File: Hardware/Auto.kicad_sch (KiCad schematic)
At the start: 30 parts, among them J10 M2, J11 M3, J12 M4, J13 HC-SR04, J9 M1, U5 74HC595, U6 TB6612FNG, U8 TB6612FNG

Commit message: Cambio borneras por SMD y elimino jumper de seleción de VS
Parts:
- J10, J11, J12, J9: footprint TerminalBlock_RND:TerminalBlock_RND_205-00287_1x02_P5.08mm_Horizontal -> footprints:CONN2_2060-452&slash_998-404_WAG; symbol Connector:Screw_Terminal_01x02 -> 2024-09-06_13-56-18:2060-452_998-404; PartNumber (none) -> 2060-452/998-404; PurchaseLink (none) -> https://www.digikey.com/en/products/detail/wago-corporation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
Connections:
- net at C16.2, J11.1 (1_1), U6.1 (AO1)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: now also J11.2 (1_2)
- net at C16.1, U6.5 (AO2), U6.6 (AO2): now also J11.3 (2_1), J11.4 (2_2); no longer J11.2 (Pin_2)
- net at C24.2, J10.1 (1_1), U8.1 (AO1)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: now also J10.2 (1_2)
- net at C25.2, U8.11 (BO1), U8.12 (BO1): now also J9.3 (2_1), J9.4 (2_2); no longer J9.2 (Pin_2)
- net at C24.1, U8.5 (AO2), U8.6 (AO2): now also J10.3 (2_1), J10.4 (2_2); no longer J10.2 (Pin_2)
- net at C25.1, J9.1 (1_1), U8.7 (BO2)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: now also J9.2 (1_2)
- net at C17.1, J12.1 (1_1), U6.7 (BO2)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: now also J12.2 (1_2)
- net at C17.2, U6.11 (BO1), U6.12 (BO1): now also J12.3 (2_1), J12.4 (2_2); no longer J12.2 (Pin_2)

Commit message: Cambio todos los conectores a SMD
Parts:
- J13: footprint Connector_PinHeader_2.54mm:PinHeader_1x04_P2.54mm_Vertical -> footprints:AMPHENOL_91601-304ALF; PartNumber (none) -> 91601-304ALF; PurchaseLink (none) -> https://www.digikey.com/en/products/detail/amphenol-cs-fci/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
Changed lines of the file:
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@@
 			)
 		)
-		(property "Footprint" "Connector_PinHeader_2.54mm:PinHeader_1x04_P2.54mm_Vertical"
+		(property "Footprint" "footprints:AMPHENOL_91601-304ALF"
 			(at 228.6 86.36 0)
 			(effects
@@
 			)
 		)
-		(property "Datasheet" "~"
+		(property "Datasheet" "https://cdn.amphenol-cs.com/media/wysiwyg/files/drawing/91601.pdf"
 			(at 228.6 86.36 0)
 			(effects
@@
 			)
 		)
-		(property "PartNumber" ""
+		(property "PartNumber" "91601-304ALF"
 			(at 228.6 86.36 0)
 			(effects
@@
 			)
 		)
-		(property "PurchaseLink" ""
+		(property "PurchaseLink" "https://www.digikey.com/en/products/detail/amphenol-cs-fci/91601-304ALF/1540494"
 			(at 228.6 86.36 0)
 			(effects

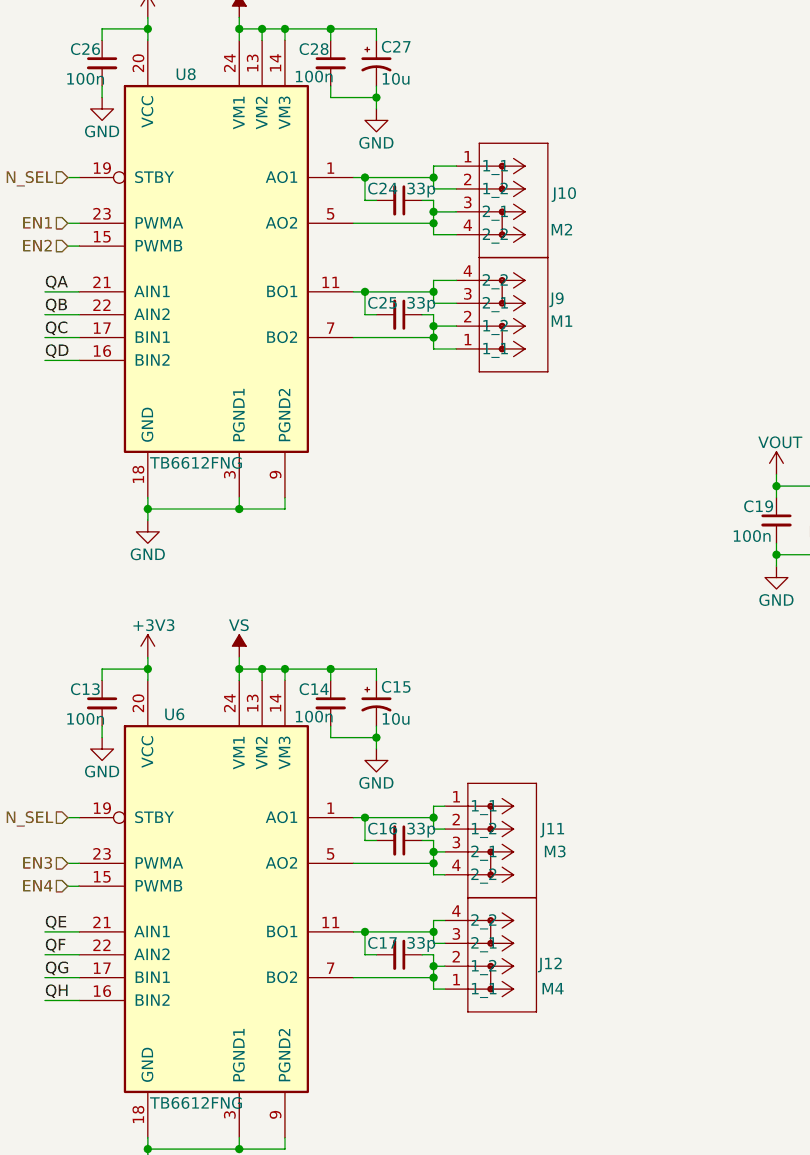
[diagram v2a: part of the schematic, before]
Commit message: Modifico error del botón en sch y ruteo pistas de potencia
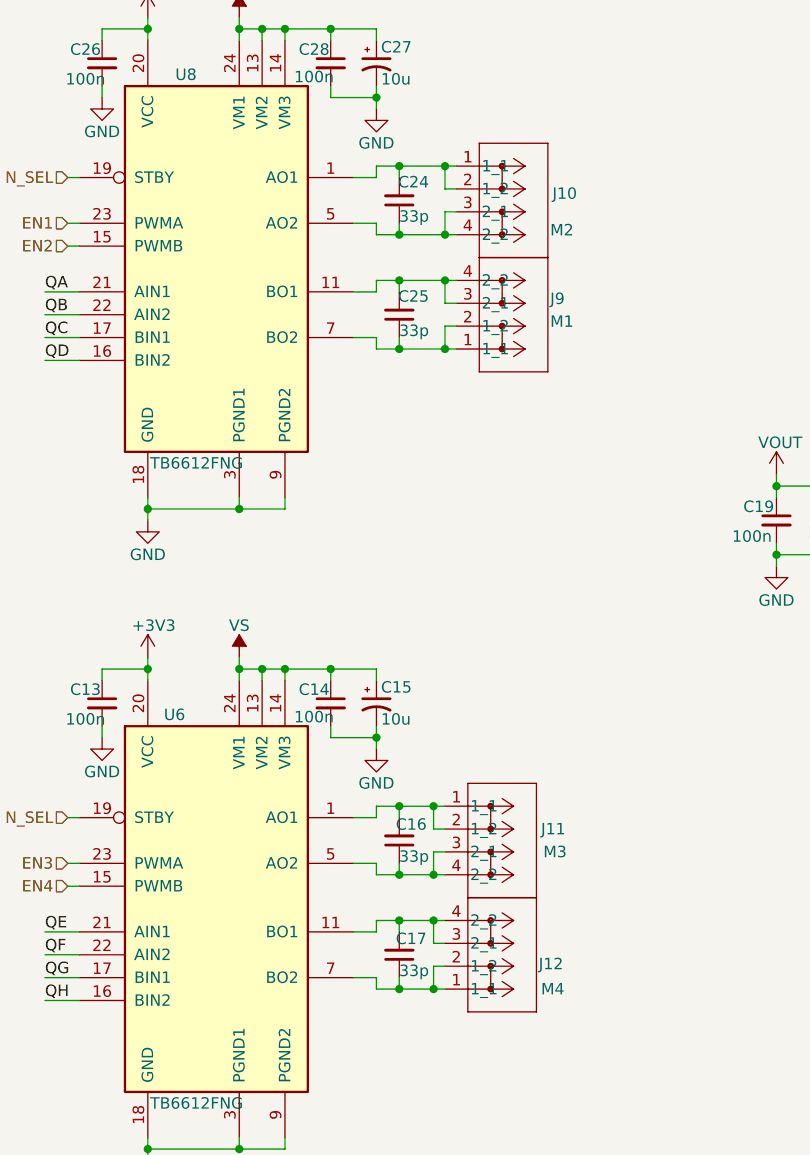
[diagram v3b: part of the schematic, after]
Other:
- moved on the sheet: C16, C17, C24, C25

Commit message: Correcciones en el ruteo, agrego fiduciales, 3D y serigrafía
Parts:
- J13: value HC-SR04 -> DISTANCIA
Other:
- company: (none) -> Newsan
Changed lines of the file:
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@@
 	(title_block
 		(title "Archi Bot")
-		(date "2024-07-18")
-		(rev "1.1")
+		(date "2024-09-27")
+		(rev "1.2")
+		(company "Newsan")
 	)
 	(junction
@@
 			)
 		)
-		(property "Value" "HC-SR04"
+		(property "Value" "DISTANCIA"
 			(at 226.822 94.234 0)
 			(effects

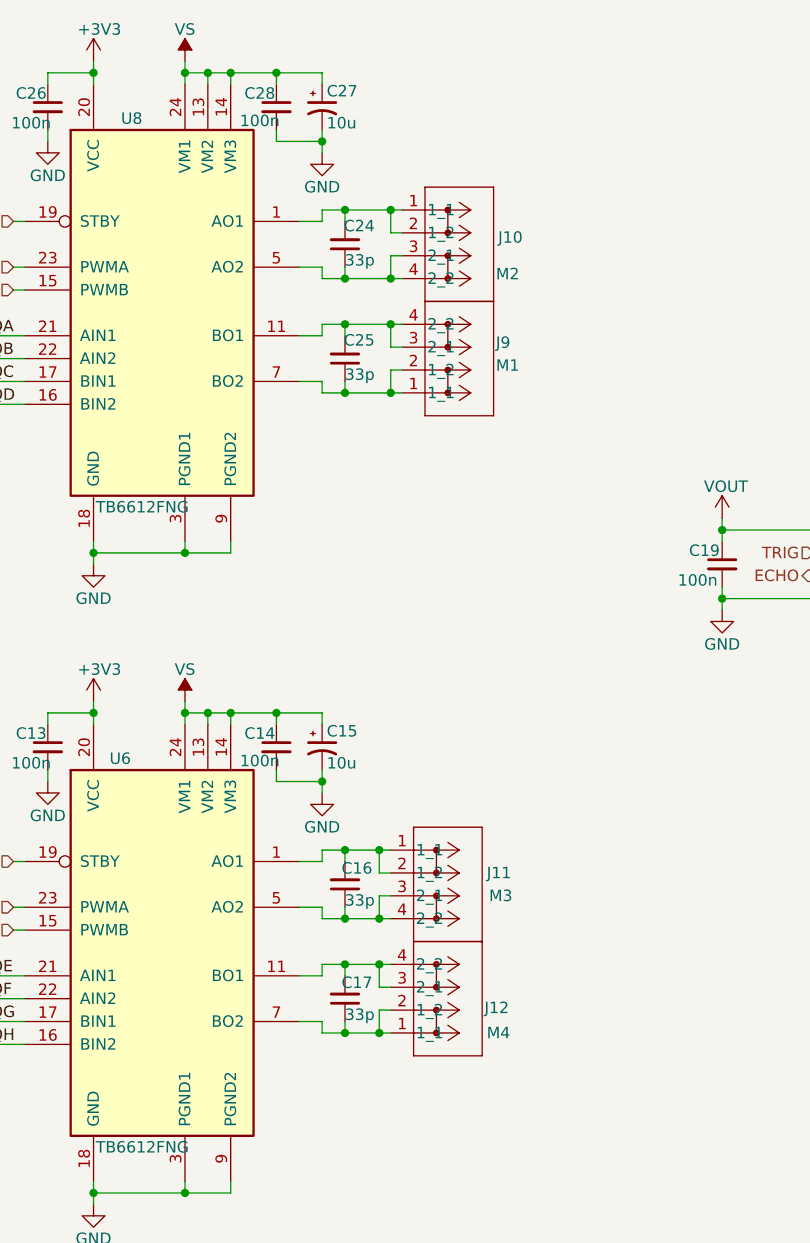
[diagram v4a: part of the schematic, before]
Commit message: Agrego test points, cambio conectores, finalizo v1.2
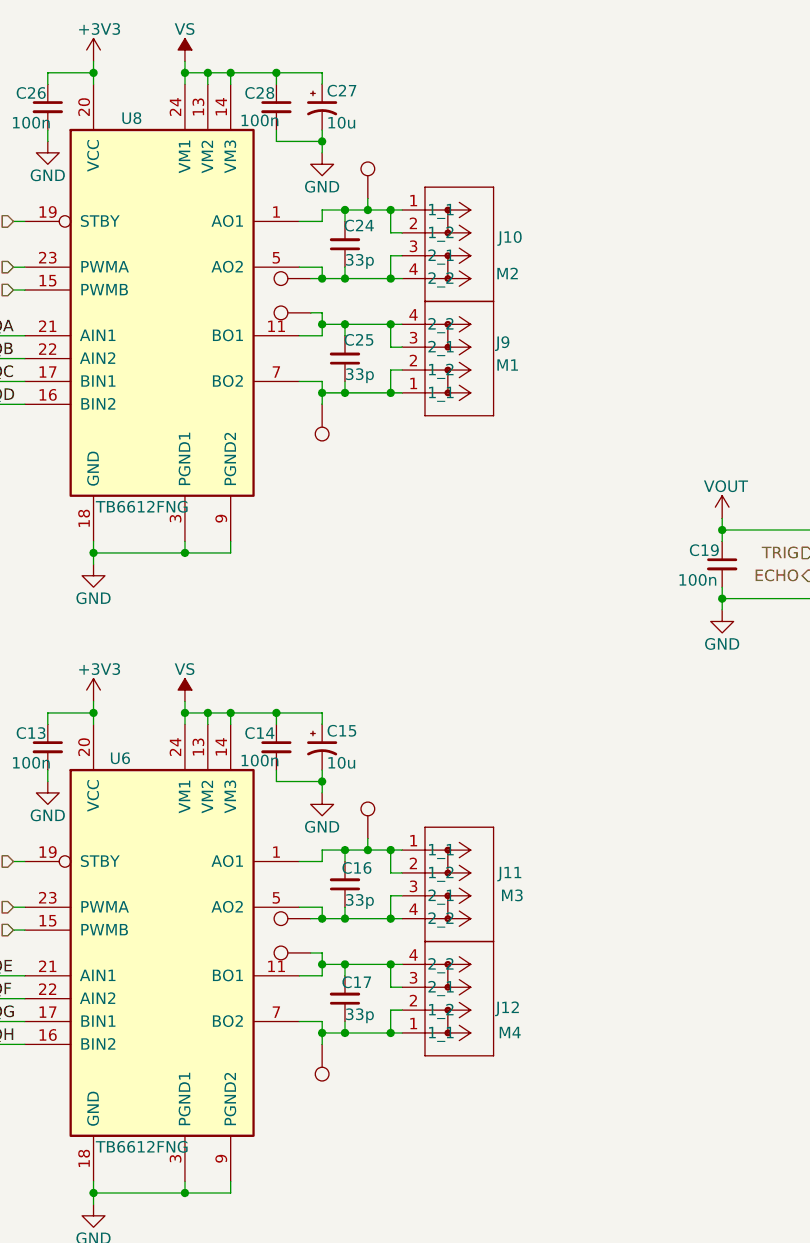
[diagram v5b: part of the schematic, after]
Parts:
- added TP20, TP21, TP22, TP23, TP24, TP25, TP26, TP27: TestPoint, TestPoint:TestPoint_Pad_D1.0mm, symbol Connector:TestPoint
- J10, J11, J12, J9: footprint footprints:CONN2_2060-452&slash_998-404_WAG -> footprints:CONN2_2060-1452&slash_998-404_WAG
- J13: footprint footprints:AMPHENOL_91601-304ALF -> footprints:AMPHENOL_91601-304ALF_modif
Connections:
- net at C16.2, J11.1 (1_1), J11.2 (1_2)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: now also TP24.1
- net at C16.1, J11.3 (2_1), J11.4 (2_2)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: now also TP25.1
- net at C24.2, J10.1 (1_1), J10.2 (1_2)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: now also TP20.1
- net at C25.2, J9.3 (2_1), J9.4 (2_2)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: now also TP22.1
- net at C24.1, J10.3 (2_1), J10.4 (2_2)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: now also TP21.1
- net at C25.1, J9.1 (1_1), J9.2 (1_2)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: now also TP23.1
- net at C17.1, J12.1 (1_1), J12.2 (1_2)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: now also TP27.1
- net at C17.2, J12.3 (2_1), J12.4 (2_2)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: now also TP26.1
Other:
- moved on the sheet: J11, J12

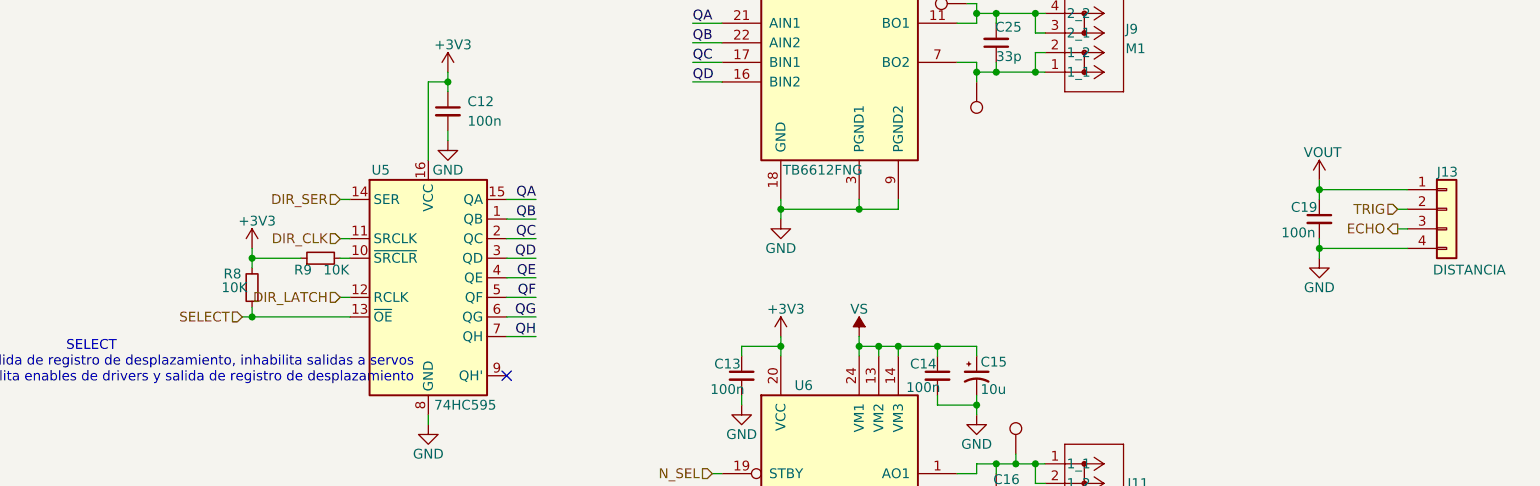
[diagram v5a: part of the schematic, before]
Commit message: Agrego testpoints y modifico footprint de bornera
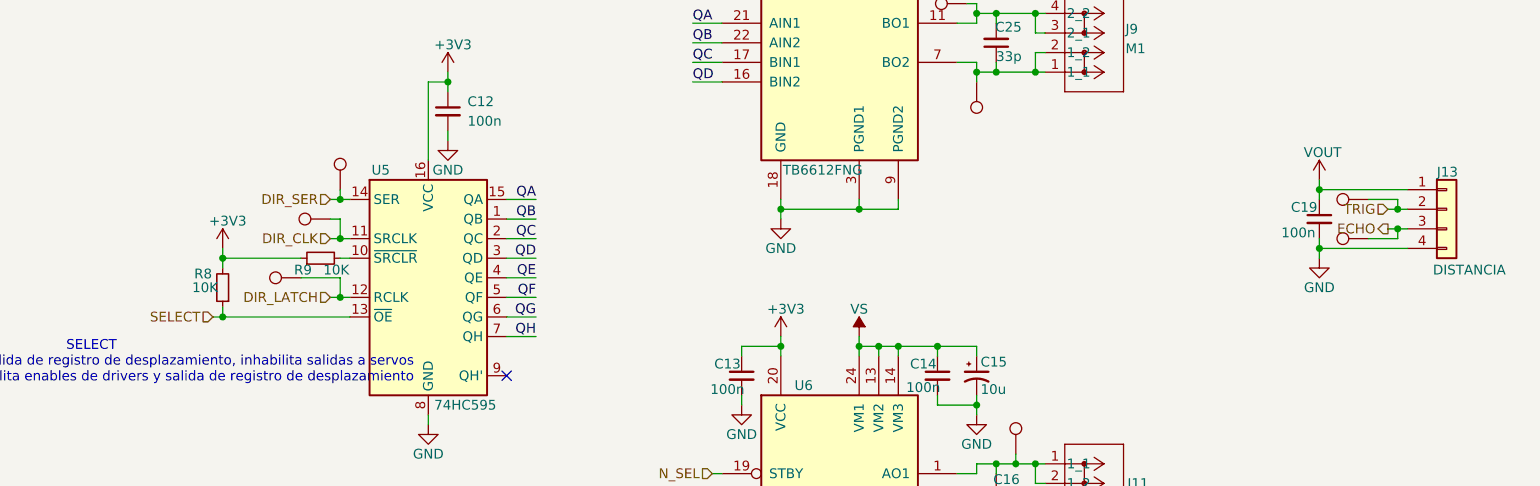
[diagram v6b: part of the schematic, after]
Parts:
- added TP32, TP33, TP34, TP35, TP36: TestPoint, TestPoint:TestPoint_Pad_D1.0mm, symbol Connector:TestPoint
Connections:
- net DIR_CLK: now also TP33.1
- net DIR_LATCH: now also TP34.1
- net DIR_SER: now also TP32.1
- net ECHO: now also TP36.1
- net TRIG: now also TP35.1
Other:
- moved on the sheet: R8

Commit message: Actualizo campo descripción
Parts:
- J10, J11, J12, J9: PartNumber 2060-452/998-404 -> 2060-1452/998-404
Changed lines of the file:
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@@
 			)
 		)
-		(property "Description" "Resistor, small symbol"
+		(property "Description" "RES 10K OHM 1% 1/10W 0603"
 			(at 95.25 151.13 0)
 			(effects
@@
 			)
 		)
-		(property "Description" "Unpolarized capacitor, small symbol"
+		(property "Description" "CAP CER 0.1UF 50V X7R 0603"
 			(at 162.56 107.95 0)
 			(effects
@@
 			)
 		)
-		(property "Description" "Resistor, small symbol"
+		(property "Description" "RES 10K OHM 1% 1/10W 0603"
 			(at 95.25 156.21 0)
 			(effects
@@
 			)
 		)
-		(property "Description" "Generic screw terminal, single row, 01x02, script generated (kicad-library-utils/schlib/autogen/connector/)"
+		(property "Description" "THR PCB TERMINAL BLOCK; PUSH-BUT 4MM"
 			(at 173.99 119.38 0)
 			(effects
@@
 			)
 		)
-		(property "PartNumber" "2060-452/998-404"
+		(property "PartNumber" "2060-1452/998-404"
 			(at 176.53 119.38 0)
 			(effects
@@
 			)
 		)
-		(property "Description" "Resistor, small symbol"
+		(property "Description" "RES 10K OHM 1% 1/10W 0603"
 			(at 95.25 130.81 0)
 			(effects
@@
 			)
 		)
-		(property "Description" "Driver IC for Dual DC motor, SSOP-24"
+		(property "Description" "IC MOTOR DRIVER 2.7V-5.5V 24SSOP"
 			(at 149.86 59.69 0)
 			(effects
@@
 			)
 		)
-		(property "Description" "Unpolarized capacitor, small symbol"
+		(property "Description" "CAP CER 33PF 50V C0G/NP0 0402"
 			(at 170.18 135.89 0)
 			(effects
@@
 			)
 		)
-		(property "Description" "Unpolarized capacitor, small symbol"
+		(property "Description" "CAP CER 33PF 50V C0G/NP0 0402"
 			(at 170.18 123.19 0)
 			(effects
@@
 			)
 		)
-		(property "Description" "Resistor, small symbol"
+		(property "Description" "RES 10K OHM 1% 1/10W 0603"
 			(at 95.25 161.29 0)
 			(effects
@@
 			)
 		)
-		(property "Description" "Unpolarized capacitor, small symbol"
+		(property "Description" "CAP CER 0.1UF 50V X7R 0603"
 			(at 212.09 87.63 0)
 			(effects
@@
 			)
 		)
-		(property "Description" "Generic connector, single row, 01x04, script generated (kicad-library-utils/schlib/autogen/connector/)"
+		(property "Description" "CONN RCPT 4POS 0.1 GOLD SMD"
 			(at 228.6 86.36 0)
 			(effects
@@
 			)
 		)
-		(property "Description" "Unpolarized capacitor, small symbol"
+		(property "Description" "CAP CER 0.1UF 50V X7R 0603"
 			(at 99.06 73.66 0)
 			(effects
@@
 			)
 		)
-		(property "Description" "Unpolarized capacitor, small symbol"
+		(property "Description" "CAP CER 33PF 50V C0G/NP0 0402"
 			(at 170.18 64.77 0)
 			(effects
@@
 			)
 		)
-		(property "Description" "Resistor, small symbol"
+		(property "Description" "RES 10K OHM 1% 1/10W 0603"
 			(at 82.55 92.71 0)
 			(effects
@@
 			)
 		)
-		(property "Description" "Resistor, small symbol"
+		(property "Description" "RES 10K OHM 1% 1/10W 0603"
 			(at 95.25 146.05 0)
 			(effects
@@
 			)
 		)
-		(property "Description" "Resistor, small symbol"
+		(property "Description" "RES 10K OHM 1% 1/10W 0603"
 			(at 95.25 140.97 0)
 			(effects
@@
 			)
 		)
-		(property "Description" "Resistor, small symbol"
+		(property "Description" "RES 10K OHM 1% 1/10W 0603"
 			(at 95.25 166.37 0)
 			(effects
@@
 			)
 		)
-		(property "Description" "Unpolarized capacitor, small symbol"
+		(property "Description" "CAP CER 0.1UF 50V X7R 0603"
 			(at 162.56 36.83 0)
 			(effects
@@
 			)
 		)
-		(property "Description" "Unpolarized capacitor, small symbol"
+		(property "Description" "CAP CER 33PF 50V C0G/NP0 0402"
 			(at 170.18 52.07 0)
 			(effects
@@
 			)
 		)
-		(property "Description" "Polarized capacitor, small US symbol"
+		(property "Description" "CAP ALUM POLY 10UF 20% 25V SMD"
 			(at 167.64 107.95 0)
 			(effects
@@
 			)
 		)
-		(property "Description" "Unpolarized capacitor, small symbol"
+		(property "Description" "CAP CER 0.1UF 50V X7R 0603"
 			(at 137.16 107.95 0)
 			(effects
@@
 			)
 		)
-		(property "Description" "Generic screw terminal, single row, 01x02, script generated (kicad-library-utils/schlib/autogen/connector/)"
+		(property "Description" "THR PCB TERMINAL BLOCK; PUSH-BUT 4MM"
 			(at 173.99 68.58 0)
 			(effects
@@
 			)
 		)
-		(property "PartNumber" "2060-452/998-404"
+		(property "PartNumber" "2060-1452/998-404"
 			(at 176.53 68.58 0)
 			(effects
@@
 			)
 		)
-		(property "Description" "Unpolarized capacitor, small symbol"
+		(property "Description" "CAP CER 0.1UF 50V X7R 0603"
 			(at 137.16 36.83 0)
 			(effects
@@
 			)
 		)
-		(property "Description" "Generic screw terminal, single row, 01x02, script generated (kicad-library-utils/schlib/autogen/connector/)"
+		(property "Description" "THR PCB TERMINAL BLOCK; PUSH-BUT 4MM"
 			(at 173.99 139.7 0)
 			(effects
@@
 			)
 		)
-		(property "PartNumber" "2060-452/998-404"
+		(property "PartNumber" "2060-1452/998-404"
 			(at 176.53 139.7 0)
 			(effects
@@
 			)
 		)
-		(property "Description" "Polarized capacitor, small US symbol"
+		(property "Description" "CAP ALUM POLY 10UF 20% 25V SMD"
 			(at 167.64 36.83 0)
 			(effects
@@
 			)
 		)
-		(property "Description" "Driver IC for Dual DC motor, SSOP-24"
+		(property "Description" "IC MOTOR DRIVER 2.7V-5.5V 24SSOP"
 			(at 149.86 130.81 0)
 			(effects
@@
 			)
 		)
-		(property "Description" "8-bit serial in/out Shift Register 3-State Outputs"
+		(property "Description" "IC SHIFT REGISTER 8BIT 16TSSOP"
 			(at 96.52 95.25 0)
 			(effects
@@
 			)
 		)
-		(property "Description" "Resistor, small symbol"
+		(property "Description" "RES 10K OHM 1% 1/10W 0603"
 			(at 95.25 135.89 0)
 			(effects
@@
 			)
 		)
-		(property "Description" "Resistor, small symbol"
+		(property "Description" "RES 10K OHM 1% 1/10W 0603"
 			(at 69.85 96.52 0)
 			(effects
@@
 			)
 		)
-		(property "Description" "Generic screw terminal, single row, 01x02, script generated (kicad-library-utils/schlib/autogen/connector/)"
+		(property "Description" "THR PCB TERMINAL BLOCK; PUSH-BUT 4MM"
 			(at 173.99 48.26 0)
 			(effects
@@
 			)
 		)
-		(property "PartNumber" "2060-452/998-404"
+		(property "PartNumber" "2060-1452/998-404"
 			(at 176.53 48.26 0)
 			(effects

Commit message: Agrego campos manufacturer y package
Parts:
- C12, C13, C14, C19, C26, C28: Manufacturer (none) -> Samsung Electro-Mechanics; Package (none) -> 0603 (1608 Metric)
- C15, C27: Manufacturer (none) -> Würth Elektronik; Package (none) -> Radial, Can - SMD (6.60mm x 6.60mm)
- C16, C17, C24, C25: Manufacturer (none) -> Murata Electronics; Package (none) -> 0402 (1005 Metric)
- J10, J11, J12, J9: Manufacturer (none) -> WAGO Corporation; Package (none) -> 0.157" (4.00mm)
- J13: Manufacturer (none) -> Amphenol ICC (FCI); Package (none) -> 4POS 0.100" (2.54mm)
- R10, R11, R12, R13, R14, R15, R16, R17, R8, R9: Manufacturer (none) -> YAGEO; Package (none) -> 0603 (1608 Metric)
- U5: Manufacturer (none) -> Nexperia USA Inc.; Package (none) -> 16-TSSOP (0.173", 4.40mm Width)
- U6, U8: Manufacturer (none) -> Toshiba Semiconductor and Storage; Package (none) -> 24-LSSOP (0.220", 5.60mm Width)
